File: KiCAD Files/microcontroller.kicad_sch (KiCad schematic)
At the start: 46 parts, among them IC5 AZ1117IH-3.3TRG1, J3 TSW-103-14-S-D, J4 TSW-103-14-S-D, J7 TSW-105-05-F-S, U1 STM32H7A3RGTx, Y1 ABM8G-48.000MHZ-18-D2Y-T

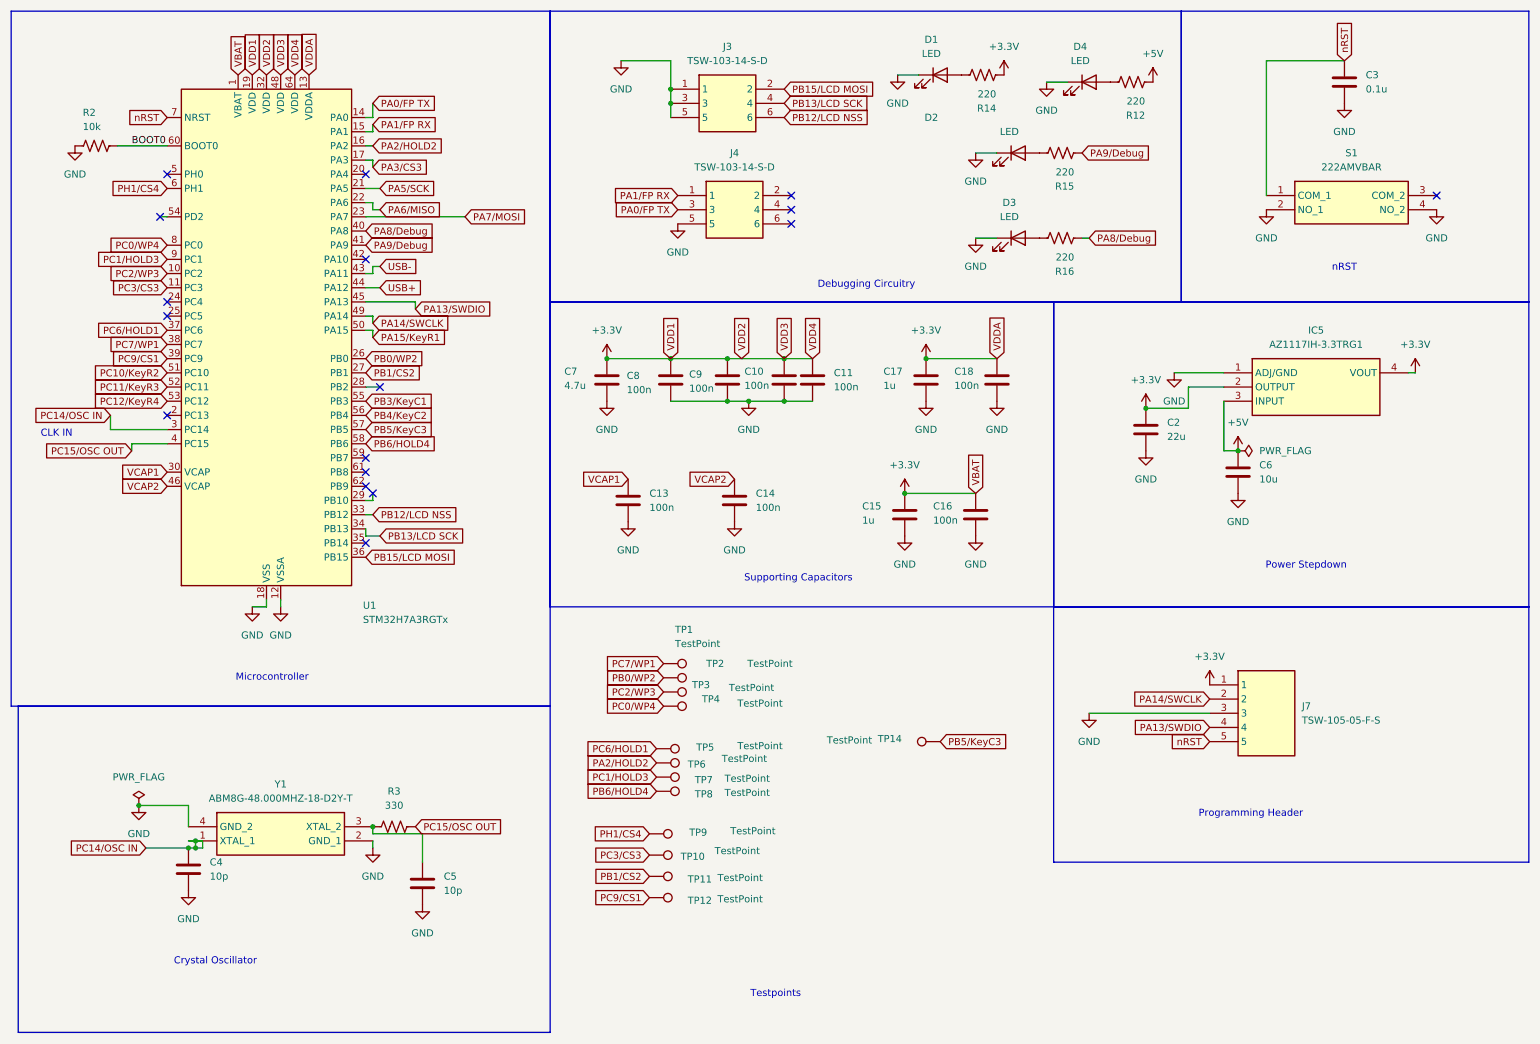
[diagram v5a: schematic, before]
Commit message: added esd changes to schematic and pcb, mainly for J1 and J5, no DRC run
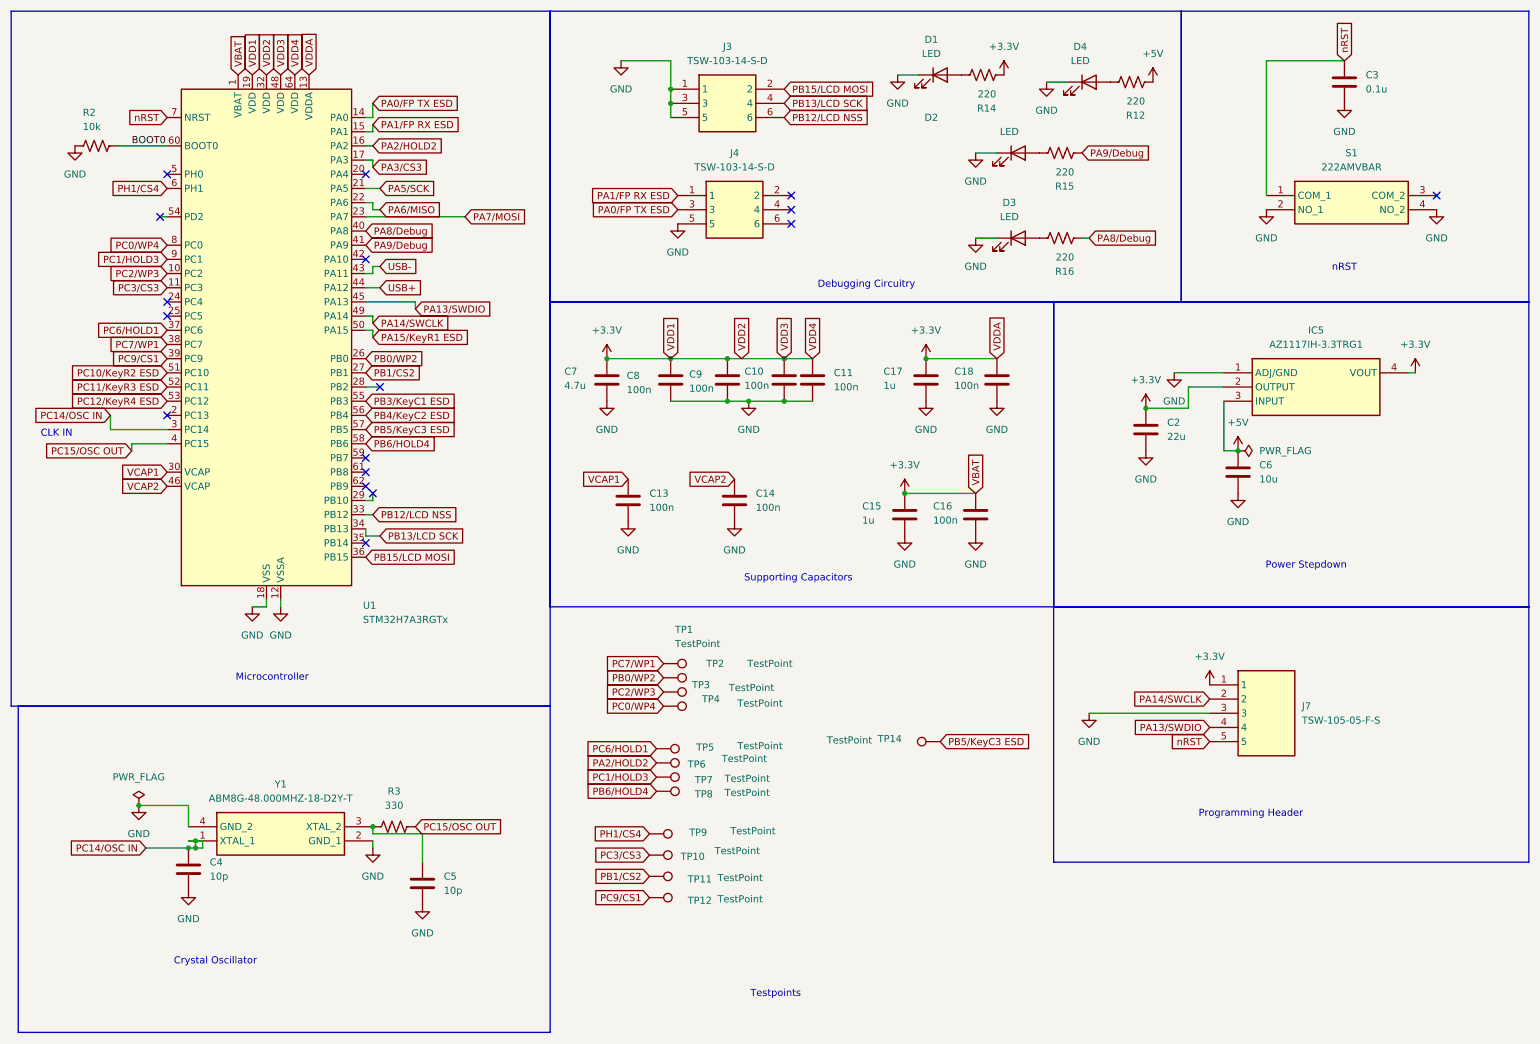
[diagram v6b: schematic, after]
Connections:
- net PA0/FP TX renamed PA0/FP TX ESD
- net PA15/KeyR1 renamed PA15/KeyR1 ESD
- net PA1/FP RX renamed PA1/FP RX ESD
- net PB3/KeyC1 renamed PB3/KeyC1 ESD
- net PB4/KeyC2 renamed PB4/KeyC2 ESD
- net PB5/KeyC3 renamed PB5/KeyC3 ESD
- net PC10/KeyR2 renamed PC10/KeyR2 ESD
- net PC11/KeyR3 renamed PC11/KeyR3 ESD
- net PC12/KeyR4 renamed PC12/KeyR4 ESD
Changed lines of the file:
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@@
 		)
 	)
-	(global_label "PB5{slash}KeyC3"
+	(global_label "PB5{slash}KeyC3 ESD"
 		(shape input)
 		(at 76.2 87.63 0)
@@
 		)
 		(property "Intersheetrefs" "${INTERSHEET_REFS}"
-			(at 90.0709 87.63 0)
+			(at 94.667 87.63 0)
 			(effects
 				(font
@@
 		)
 	)
-	(global_label "PB5{slash}KeyC3"
+	(global_label "PB5{slash}KeyC3 ESD"
 		(shape input)
 		(at 179.07 143.51 0)
@@
 		)
 		(property "Intersheetrefs" "${INTERSHEET_REFS}"
-			(at 192.9409 143.51 0)
+			(at 197.537 143.51 0)
 			(effects
 				(font
@@
 		)
 	)
-	(global_label "PA0{slash}FP TX"
+	(global_label "PA0{slash}FP TX ESD"
 		(shape input)
 		(at 132.08 48.26 180)
@@
 		)
 		(property "Intersheetrefs" "${INTERSHEET_REFS}"
-			(at 118.6929 48.26 0)
+			(at 114.0968 48.26 0)
 			(effects
 				(font
@@
 		)
 	)
-	(global_label "PC12{slash}KeyR4"
+	(global_label "PC12{slash}KeyR4 ESD"
 		(shape input)
 		(at 40.64 82.55 180)
@@
 		)
 		(property "Intersheetrefs" "${INTERSHEET_REFS}"
-			(at 25.5596 82.55 0)
+			(at 20.9635 82.55 0)
 			(effects
 				(font
@@
 		)
 	)
-	(global_label "PB4{slash}KeyC2"
+	(global_label "PB4{slash}KeyC2 ESD"
 		(shape input)
 		(at 76.2 85.09 0)
@@
 		)
 		(property "Intersheetrefs" "${INTERSHEET_REFS}"
-			(at 90.0709 85.09 0)
-			(effects
-				(font
-					(size 1.27 1.27)
-				)
-				(justify left)
-				(hide yes)
-			)
-		)
-	)
-	(global_label "PA15{slash}KeyR1"
+			(at 94.667 85.09 0)
+			(effects
+				(font
+					(size 1.27 1.27)
+				)
+				(justify left)
+				(hide yes)
+			)
+		)
+	)
+	(global_label "PA15{slash}KeyR1 ESD"
 		(shape input)
 		(at 77.47 71.12 0)
@@
 		)
 		(property "Intersheetrefs" "${INTERSHEET_REFS}"
-			(at 92.369 71.12 0)
+			(at 96.9651 71.12 0)
 			(effects
 				(font
@@
 		)
 	)
-	(global_label "PA1{slash}FP RX"
+	(global_label "PA1{slash}FP RX ESD"
 		(shape input)
 		(at 77.47 33.02 0)
@@
 		)
 		(property "Intersheetrefs" "${INTERSHEET_REFS}"
-			(at 91.1595 33.02 0)
+			(at 95.7556 33.02 0)
 			(effects
 				(font
@@
 		)
 	)
-	(global_label "PA0{slash}FP TX"
+	(global_label "PA0{slash}FP TX ESD"
 		(shape input)
 		(at 77.47 29.21 0)
@@
 		)
 		(property "Intersheetrefs" "${INTERSHEET_REFS}"
-			(at 90.8571 29.21 0)
+			(at 95.4532 29.21 0)
 			(effects
 				(font
@@
 		)
 	)
-	(global_label "PC11{slash}KeyR3"
+	(global_label "PC11{slash}KeyR3 ESD"
 		(shape input)
 		(at 40.64 80.01 180)
@@
 		)
 		(property "Intersheetrefs" "${INTERSHEET_REFS}"
-			(at 25.5596 80.01 0)
+			(at 20.9635 80.01 0)
 			(effects
 				(font
@@
 		)
 	)
-	(global_label "PB3{slash}KeyC1"
+	(global_label "PB3{slash}KeyC1 ESD"
 		(shape input)
 		(at 76.2 82.55 0)
@@
 		)
 		(property "Intersheetrefs" "${INTERSHEET_REFS}"
-			(at 90.0709 82.55 0)
+			(at 94.667 82.55 0)
 			(effects
 				(font
@@
 		)
 	)
-	(global_label "PC10{slash}KeyR2"
+	(global_label "PC10{slash}KeyR2 ESD"
 		(shape input)
 		(at 40.64 77.47 180)
@@
 		)
 		(property "Intersheetrefs" "${INTERSHEET_REFS}"
-			(at 25.5596 77.47 0)
-			(effects
-				(font
-					(size 1.27 1.27)
-				)
-				(justify right)
-				(hide yes)
-			)
-		)
-	)
-	(global_label "PA1{slash}FP RX"
+			(at 20.9635 77.47 0)
+			(effects
+				(font
+					(size 1.27 1.27)
+				)
+				(justify right)
+				(hide yes)
+			)
+		)
+	)
+	(global_label "PA1{slash}FP RX ESD"
 		(shape input)
 		(at 132.08 45.72 180)
@@
 		)
 		(property "Intersheetrefs" "${INTERSHEET_REFS}"
-			(at 118.3905 45.72 0)
-			(effects
-				(font
+			(at 113.7944 45.72 0)
+			(effects
+				(font

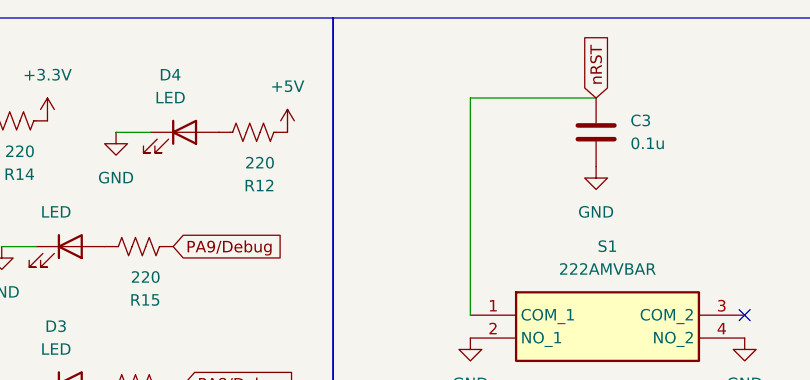
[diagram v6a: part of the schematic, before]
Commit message: added pullup for nrst and fixed drc warnings for silkscreen
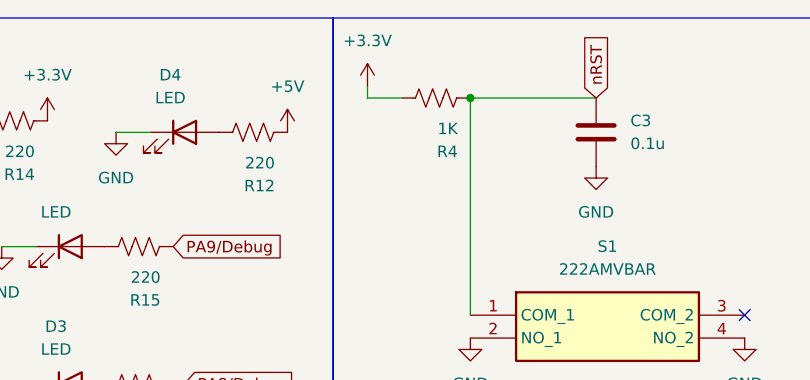
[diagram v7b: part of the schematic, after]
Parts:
- added R4: 1K, Resistor_SMD:R_0805_2012Metric_Pad1.20x1.40mm_HandSolder, symbol CustomSymbols:R_US
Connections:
- net +3.3V: now also R4.1
- net nRST: now also R4.2
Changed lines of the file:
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@@
 	)
 	(junction
+		(at 237.49 21.59)
+		(diameter 0)
+		(color 0 0 0 0)
+	)
+	(junction
 		(at 232.41 91.44)
 		(diameter 0)
@@
 	(wire
 		(pts
+			(xy 226.06 21.59) (xy 229.87 21.59)
+		)
+		(stroke
+			(width 0)
+			(type default)
+		)
+	)
+	(wire
+		(pts
 			(xy 237.49 45.72) (xy 237.49 21.59)
 		)
@@
 	(wire
 		(pts
+			(xy 226.06 20.32) (xy 226.06 21.59)
+		)
+		(stroke
+			(width 0)
+			(type default)
+		)
+	)
+	(wire
+		(pts
 			(xy 39.37 49.53) (xy 40.64 49.53)
 		)
@@
 	)
 	(symbol
+		(lib_id "CustomSymbols:+3.3V")
+		(at 226.06 20.32 0)
+		(unit 1)
+		(exclude_from_sim no)
+		(in_bom yes)
+		(on_board yes)
+		(dnp no)
+		(fields_autoplaced yes)
+		(property "Reference" "#PWR70"
+			(at 226.06 24.13 0)
+			(effects
+				(font
+					(size 1.27 1.27)
+				)
+				(hide yes)
+			)
+		)
+		(property "Value" "+3.3V"
+			(at 226.06 15.24 0)
+			(effects
+				(font
+					(size 1.27 1.27)
+				)
+			)
+		)
+		(property "Footprint" ""
+			(at 226.06 20.32 0)
+			(effects
+				(font
+					(size 1.27 1.27)
+				)
+				(hide yes)
+			)
+		)
+		(property "Datasheet" ""
+			(at 226.06 20.32 0)
+			(effects
+				(font
+					(size 1.27 1.27)
+				)
+				(hide yes)
+			)
+		)
+		(property "Description" "Power symbol creates a global label with name \"+3.3V\""
+			(at 226.06 20.32 0)
+			(effects
+				(font
+					(size 1.27 1.27)
+				)
+				(hide yes)
+			)
+		)
+		(pin "1"
+		)
+		(instances
+			(project "477"
+				(path "/b633f67e-3a02-4f0f-b079-02d1853b4f15/e8b68c2d-7a8c-4c60-b0ed-d46a3d1cc27a"
+					(reference "#PWR70")
+					(unit 1)
+				)
+			)
+		)
+	)
+	(symbol
 		(lib_id "CustomSymbols:GND")
 		(at 35.56 154.94 0)
@@
 					(unit 1)
 				)
+			)
+		)
+	)
+	(symbol
+		(lib_id "CustomSymbols:R_US")
+		(at 233.68 21.59 90)
+		(unit 1)
+		(exclude_from_sim no)
+		(in_bom yes)
+		(on_board yes)
+		(dnp no)
+		(property "Reference" "R4"
+			(at 236.093 27.559 90)
+			(effects
+				(font
+					(size 1.27 1.27)
+				)
+				(justify left)
+			)
+		)
+		(property "Value" "1K"
+			(at 236.093 25.019 90)
+			(effects
+				(font
+					(size 1.27 1.27)
+				)
+				(justify left)
+			)
+		)
+		(property "Footprint" "Resistor_SMD:R_0805_2012Metric_Pad1.20x1.40mm_HandSolder"
+			(at 233.934 20.574 90)
+			(effects
+				(font
+					(size 1.27 1.27)
+				)
+				(hide yes)
+			)
+		)
+		(property "Datasheet" "~"
+			(at 233.68 21.59 0)
+			(effects
+				(font
+					(size 1.27 1.27)
+				)
+				(hide yes)
+			)
+		)
+		(property "Description" "Resistor, US symbol"
+			(at 233.68 21.59 0)
+			(effects
+				(font
+					(size 1.27 1.27)
+				)
+				(hide yes)
+			)
+		)
+		(pin "1"
+		)
+		(pin "2"
+		)
+		(instances
+			(project "477"
+				(path "/b633f67e-3a02-4f0f-b079-02d1853b4f15/e8b68c2d-7a8c-4c60-b0ed-d46a3d1cc27a"
+					(reference "R4")
+					(unit 1)
+				)

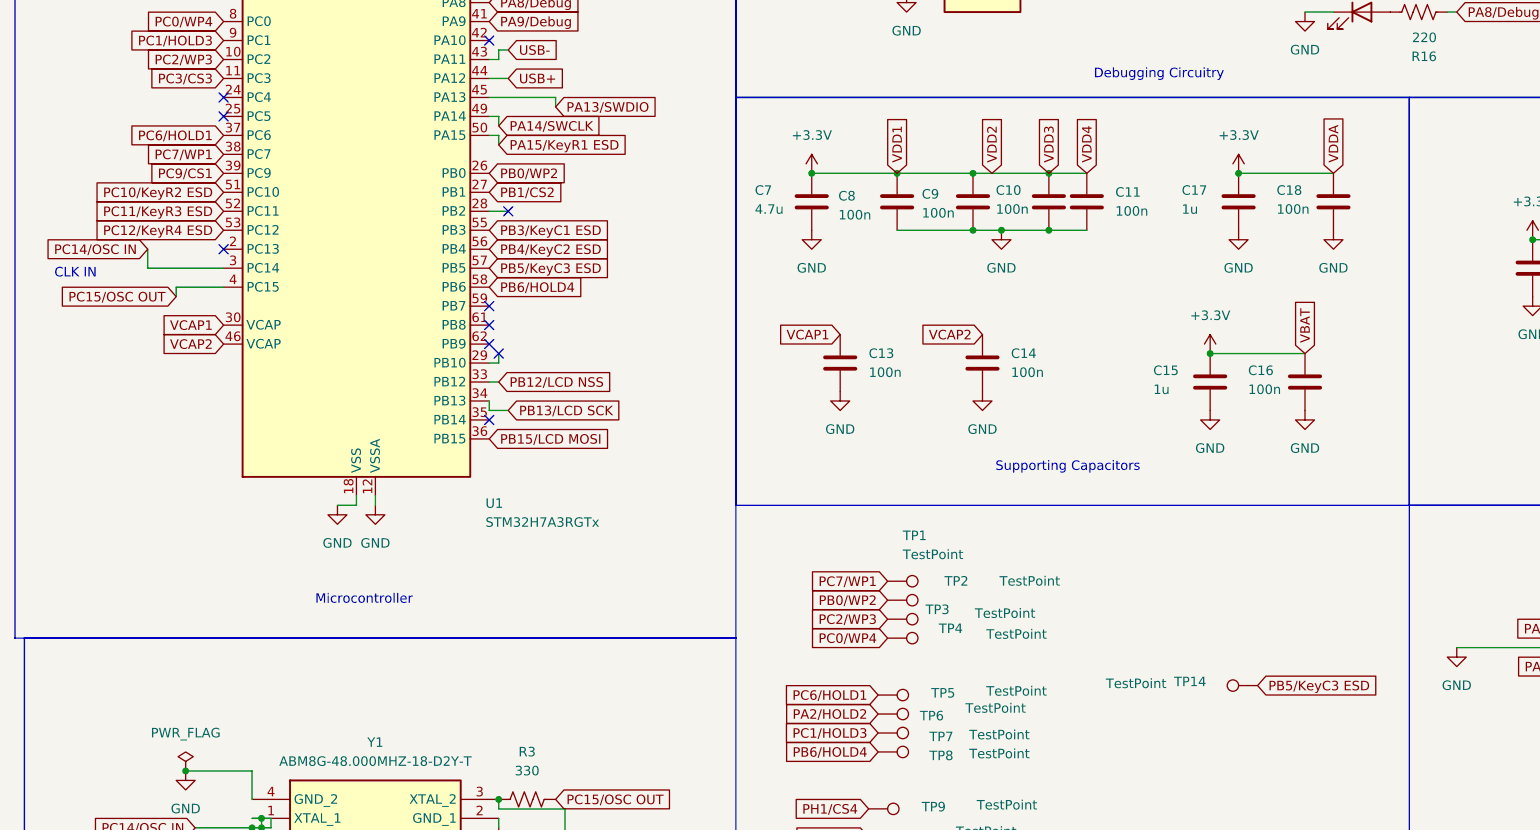
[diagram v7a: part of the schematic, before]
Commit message: updated keypad schematic
rendered testpoint useless, but keypad should not require much use of test points.
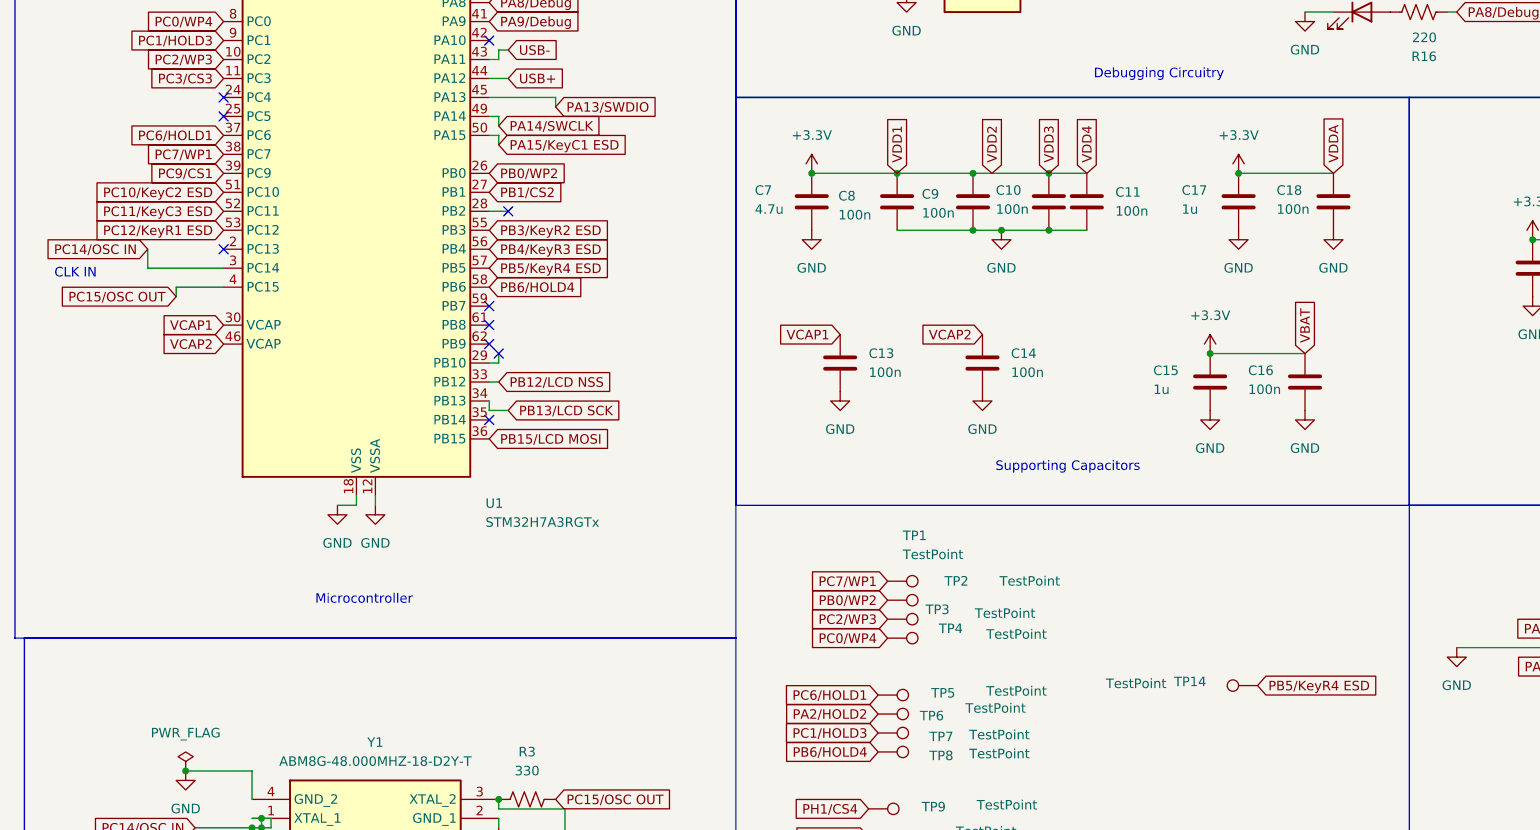
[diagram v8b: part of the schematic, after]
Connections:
- net PA15/KeyR1 ESD renamed PA15/KeyC1 ESD
- net PB3/KeyC1 ESD renamed PB3/KeyR2 ESD
- net PB4/KeyC2 ESD renamed PB4/KeyR3 ESD
- net PB5/KeyC3 ESD renamed PB5/KeyR4 ESD
- net PC10/KeyR2 ESD renamed PC10/KeyC2 ESD
- net PC11/KeyR3 ESD renamed PC11/KeyC3 ESD
- net PC12/KeyR4 ESD renamed PC12/KeyR1 ESD
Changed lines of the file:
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@@
 	(label "BOOT0"
 		(at 34.29 36.83 0)
+		(fields_autoplaced yes)
 		(effects
 			(font
@@
 		)
 	)
-	(global_label "PB5{slash}KeyC3 ESD"
+	(global_label "PB5{slash}KeyR4 ESD"
 		(shape input)
 		(at 76.2 87.63 0)
@@
 		)
 	)
-	(global_label "PB5{slash}KeyC3 ESD"
+	(global_label "PB5{slash}KeyR4 ESD"
 		(shape input)
 		(at 179.07 143.51 0)
@@
 		)
 	)
-	(global_label "PC12{slash}KeyR4 ESD"
+	(global_label "PC12{slash}KeyR1 ESD"
 		(shape input)
 		(at 40.64 82.55 180)
@@
 		)
 	)
-	(global_label "PB4{slash}KeyC2 ESD"
+	(global_label "PB4{slash}KeyR3 ESD"
 		(shape input)
 		(at 76.2 85.09 0)
@@
 		)
 	)
-	(global_label "PA15{slash}KeyR1 ESD"
+	(global_label "PA15{slash}KeyC1 ESD"
 		(shape input)
 		(at 77.47 71.12 0)
@@
 		)
 	)
-	(global_label "PC11{slash}KeyR3 ESD"
+	(global_label "PC11{slash}KeyC3 ESD"
 		(shape input)
 		(at 40.64 80.01 180)
@@
 		)
 	)
-	(global_label "PB3{slash}KeyC1 ESD"
+	(global_label "PB3{slash}KeyR2 ESD"
 		(shape input)
 		(at 76.2 82.55 0)
@@
 		)
 	)
-	(global_label "PC10{slash}KeyR2 ESD"
+	(global_label "PC10{slash}KeyC2 ESD"
 		(shape input)
 		(at 40.64 77.47 180)
@@
 		(dnp no)
 		(fields_autoplaced yes)
-		(property "Reference" "#PWR70"
+		(property "Reference" "#PWR070"
 			(at 226.06 24.13 0)
 			(effects
@@
 			(project "477"
 				(path "/b633f67e-3a02-4f0f-b079-02d1853b4f15/e8b68c2d-7a8c-4c60-b0ed-d46a3d1cc27a"
-					(reference "#PWR70")
+					(reference "#PWR070")
 					(unit 1)
 				)
